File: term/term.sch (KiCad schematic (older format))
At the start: 2 parts

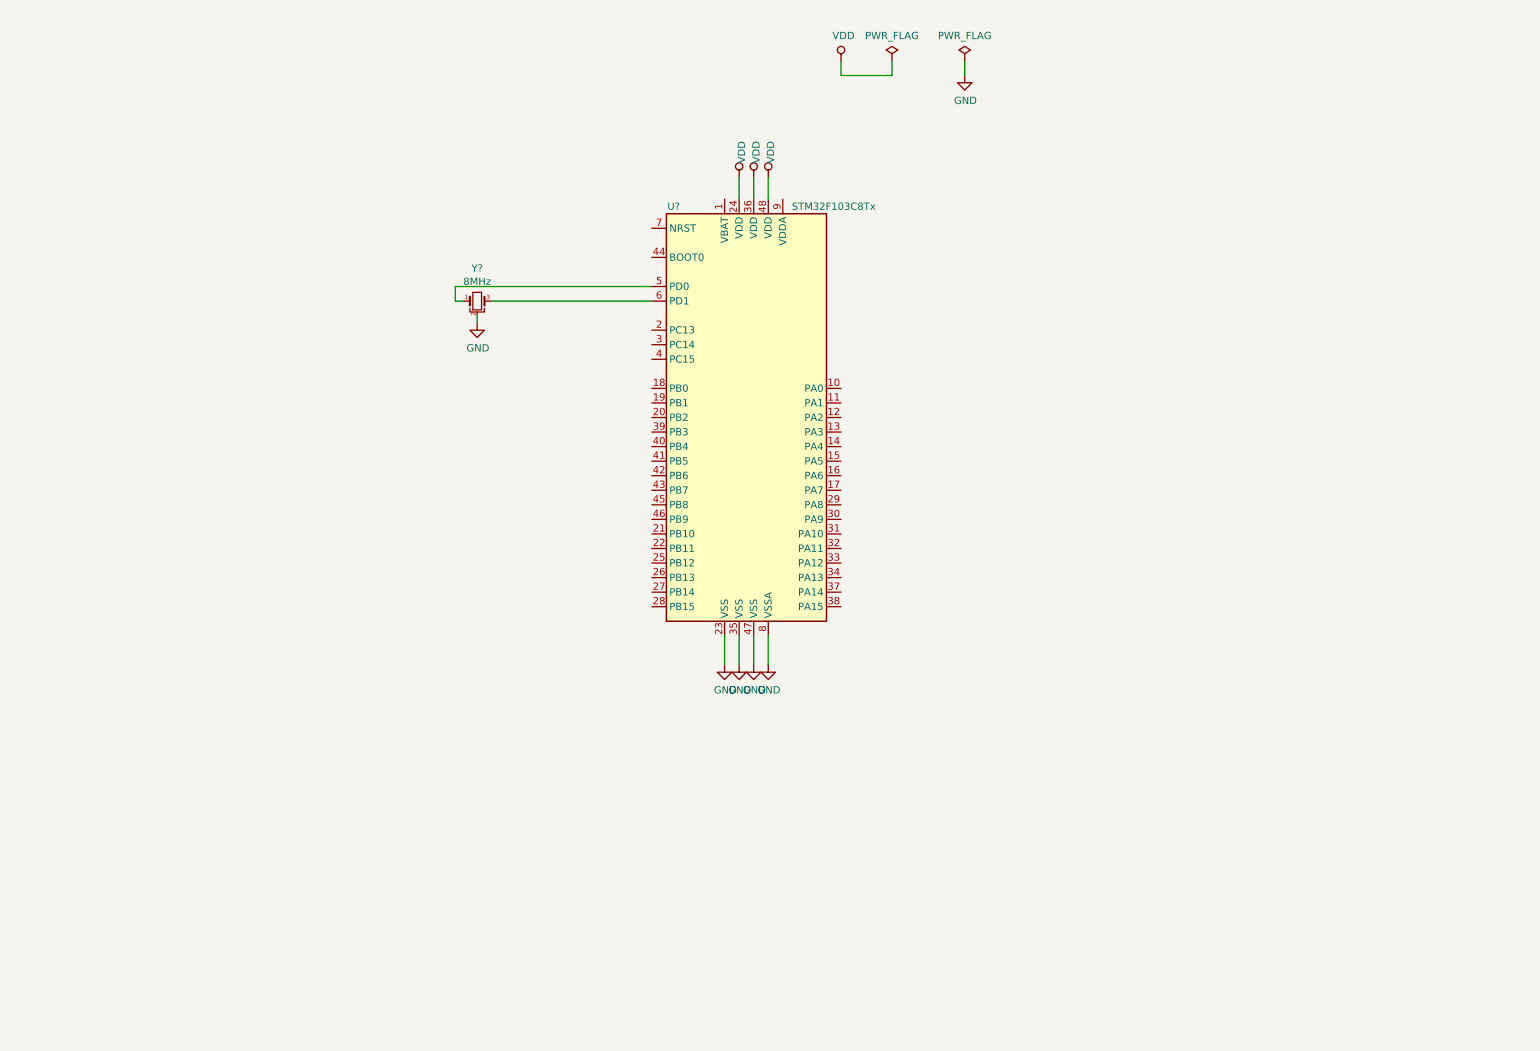
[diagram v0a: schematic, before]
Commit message: Add eeprom functions, i2c functions, save and restore data
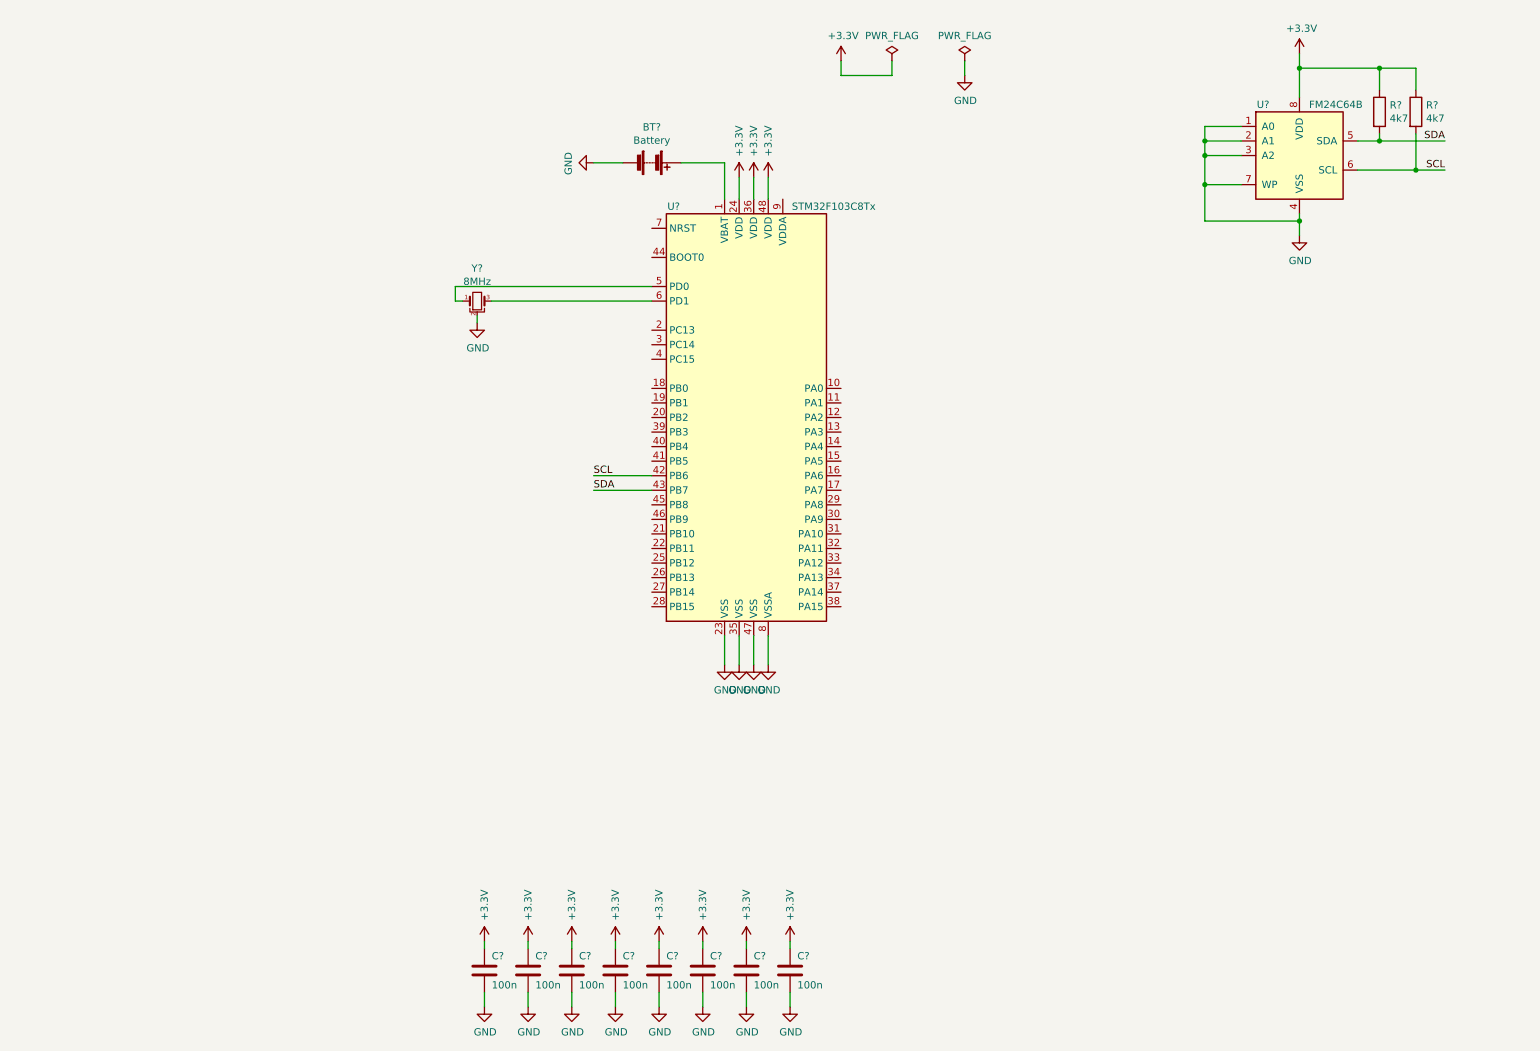
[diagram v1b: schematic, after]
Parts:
- added BT?: Battery, Battery:BatteryHolder_ComfortableElectronic_CH273-2450_1x2450, symbol Device:Battery
- added C? (x8): 100n, Capacitor_SMD:C_0805_2012Metric, symbol Device:C
- added R? (x2): 4k7, Resistor_SMD:R_0805_2012Metric, symbol Device:R
- added U?: FM24C64B, Package_SO:SOIC-8_3.9x4.9mm_P1.27mm, symbol Memory_NVRAM:FM24C64B
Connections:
- net GND: now also BT?.2 (-), C?.2, C?.2, C?.2, C?.2, C?.2, C?.2, C?.2, C?.2, U?.1 (A0), U?.2 (A1), U?.3 (A2), U?.4 (VSS), U?.7 (WP)
- net at U?.1 (VBAT): now also BT?.1 (+)
- net SCL: now reaches U?.42 (PB6)
- net SCL: now also R?.2, U?.6 (SCL)
- net SDA: now reaches U?.43 (PB7)
- net SDA: now also R?.2, U?.5 (SDA)
- net VDD renamed +3V3
- net +3V3: now also C?.1, C?.1, C?.1, C?.1, C?.1, C?.1, C?.1, C?.1, R?.1, R?.1, U?.8 (VDD)

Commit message: Continue schematic draw
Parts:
- removed R? (x2): 4k7, Resistor_SMD:R_0805_2012Metric, symbol Device:R
- added C10: 100n, Capacitor_SMD:C_0805_2012Metric, symbol Device:C_Small
- added C11, C9: 22p, Capacitor_SMD:C_0805_2012Metric, symbol Device:C_Small
- added J1, J2, J3: Conn_01x03_Male, symbol Connector:Conn_01x03_Male
- added J4: Conn_ARM_JTAG_SWD_10, Connector_IDC:IDC-Header_2x05_P2.54mm_Vertical, symbol Connector:Conn_ARM_JTAG_SWD_10
- added R1: 1k, Resistor_SMD:R_0805_2012Metric, symbol Device:R_Small
- added R2, R6, R7: 4k7, Resistor_SMD:R_0805_2012Metric, symbol Device:R_Small
- added R3: 10, Resistor_SMD:R_1210_3225Metric, symbol Device:R_Small
- added R4, R5: 100k, Resistor_SMD:R_0805_2012Metric, symbol Device:R_Small
- added RV1: 10k, symbol Device:R_POT_Small
- added U1: 74HC595, Package_SO:SOIC-16_3.9x9.9mm_P1.27mm, symbol 74xx:74HC595
- added U2: WG12864A, Connector_PinHeader_2.54mm:PinHeader_1x20_P2.54mm_Vertical, symbol lcd:WG12864A
- added Y2: 32678, symbol Device:Crystal_Small
- gave numbers to parts that had none: 12
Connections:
- net +3V3: now also J1.1 (Pin_1), J2.1 (Pin_1), J3.1 (Pin_1), J4.1 (VTref), R2.2, R4.1, R6.1, R7.1
- net GND: now also C10.2, C11.2, C9.1, J1.3 (Pin_3), J2.3 (Pin_3), J3.3 (Pin_3), J4.3 (GND), J4.5 (GND), J4.9 (GNDDetect), R3.2, R5.2, U1.13 (~OE), U1.8 (GND), U2.1 (Vss), U2.5 (R/W)
- net SCL: now also R7.2
- net SDA: now also R6.2
- net KEY_UP: now reaches U3.12 (PA2)
- net KEY_DOWN: now reaches U3.13 (PA3)
- net KEY_LEFT: now reaches U3.14 (PA4)
- net KEY_RIGHT: now reaches U3.15 (PA5)
- net OW: now reaches U3.17 (PA7)
- net OW: now also J1.2 (Pin_2), J2.2 (Pin_2), J3.2 (Pin_2), R2.1
- net LCD_RST: now reaches U3.21 (PB10)
- net LCD_RST: now also U2.17 (~RES)
- net LCD_DI: now reaches U3.22 (PB11)
- net LCD_DI: now also U2.4 (D/I)
- net LCD_CLK: now reaches U3.25 (PB12)
- net LCD_CLK: now also U1.12 (RCLK)
- net LCD_SHIFT: now reaches U3.26 (PB13)
- net LCD_SHIFT: now also U1.11 (SRCLK)
- net LCD_E: now reaches U3.27 (PB14)
- net LCD_E: now also U2.6 (E)
- net LCD_DATA: now reaches U3.28 (PB15)
- net LCD_DATA: now also U1.14 (SER)
- net at U3.3 (PC14): now also C9.2, Y2.2
- net USART1_TX: now reaches U3.30 (PA9)
- net USART1_RX: now reaches U3.31 (PA10)
- net JTMS: now reaches U3.34 (PA13)
- net JTMS: now also J4.2 (SWDIO/TMS)
- net JTCK: now reaches U3.37 (PA14)
- net JTCK: now also J4.4 (SWDCLK/TCK)
- net JTDI: now reaches U3.38 (PA15)
- net JTDI: now also J4.8 (NC/TDI)
- net JTDO: now reaches U3.39 (PB3)
- net JTDO: now also J4.6 (SWO/TDO)
- net at U3.4 (PC15): now also C11.1, Y2.1
- net at U3.44 (BOOT0): now also R5.1
- net LCD_CS1: now reaches U3.45 (PB8)
- net LCD_CS1: now also U2.15 (CS1)
- net LCD_CS2: now reaches U3.46 (PB9)
- net LCD_CS2: now also U2.16 (CS2)
- net NRESET: now reaches U3.7 (NRST)
- net NRESET: now also C10.1, J4.10 (~RESET~), R4.2
- new net: U1.3 (QD), U2.10 (DB3)
- new net: U1.4 (QE), U2.11 (DB4)
- new net: U1.5 (QF), U2.12 (DB5)
- new net: U1.6 (QG), U2.13 (DB6)
- new net: U1.7 (QH), U2.14 (DB7)
- new net: RV1.3, U2.18 (Vout)
- new net: R3.1, U2.20 (K)
- new net: RV1.2, U2.3 (V0)
- new net: U1.15 (QA), U2.7 (DB0)
- new net: U1.1 (QB), U2.8 (DB1)
- new net: U1.2 (QC), U2.9 (DB2)
- new net: R1.2, U1.10 (~SRCLR)
- new net VCC: R1.1, RV1.1, U1.16 (VCC), U2.19 (A), U2.2 (Vdd)
- no-connect marks 0 -> 10
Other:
- moved on the sheet: BT1, U3, U4, Y1

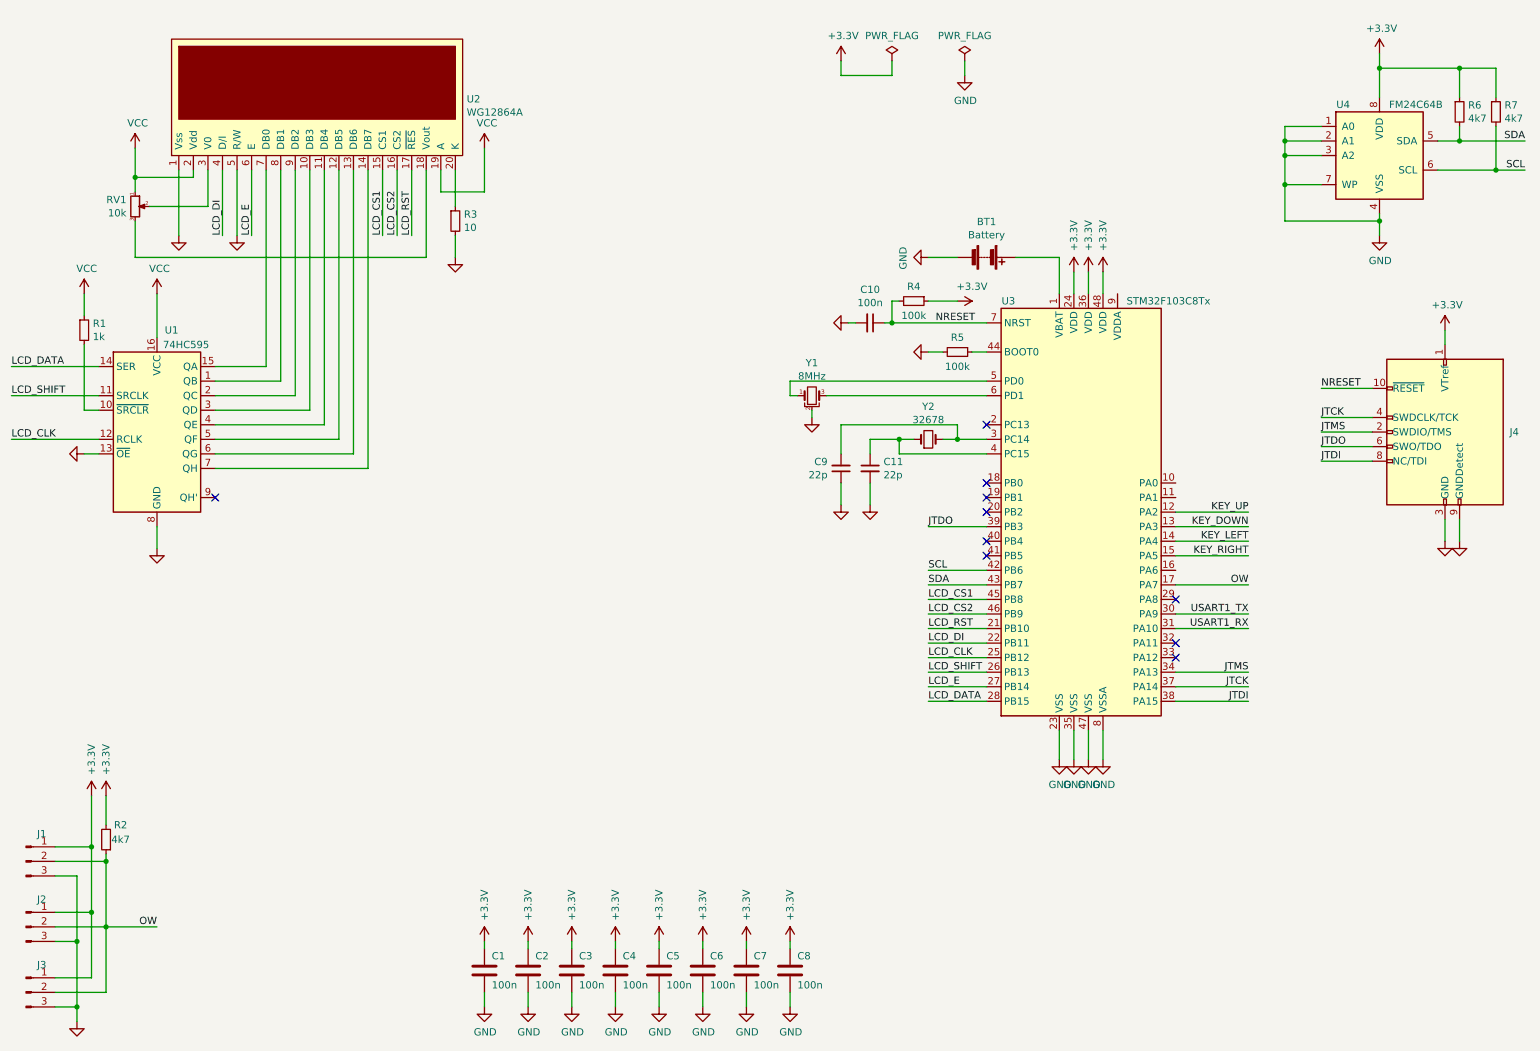
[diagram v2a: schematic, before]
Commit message: Add kicad project with stm32 module
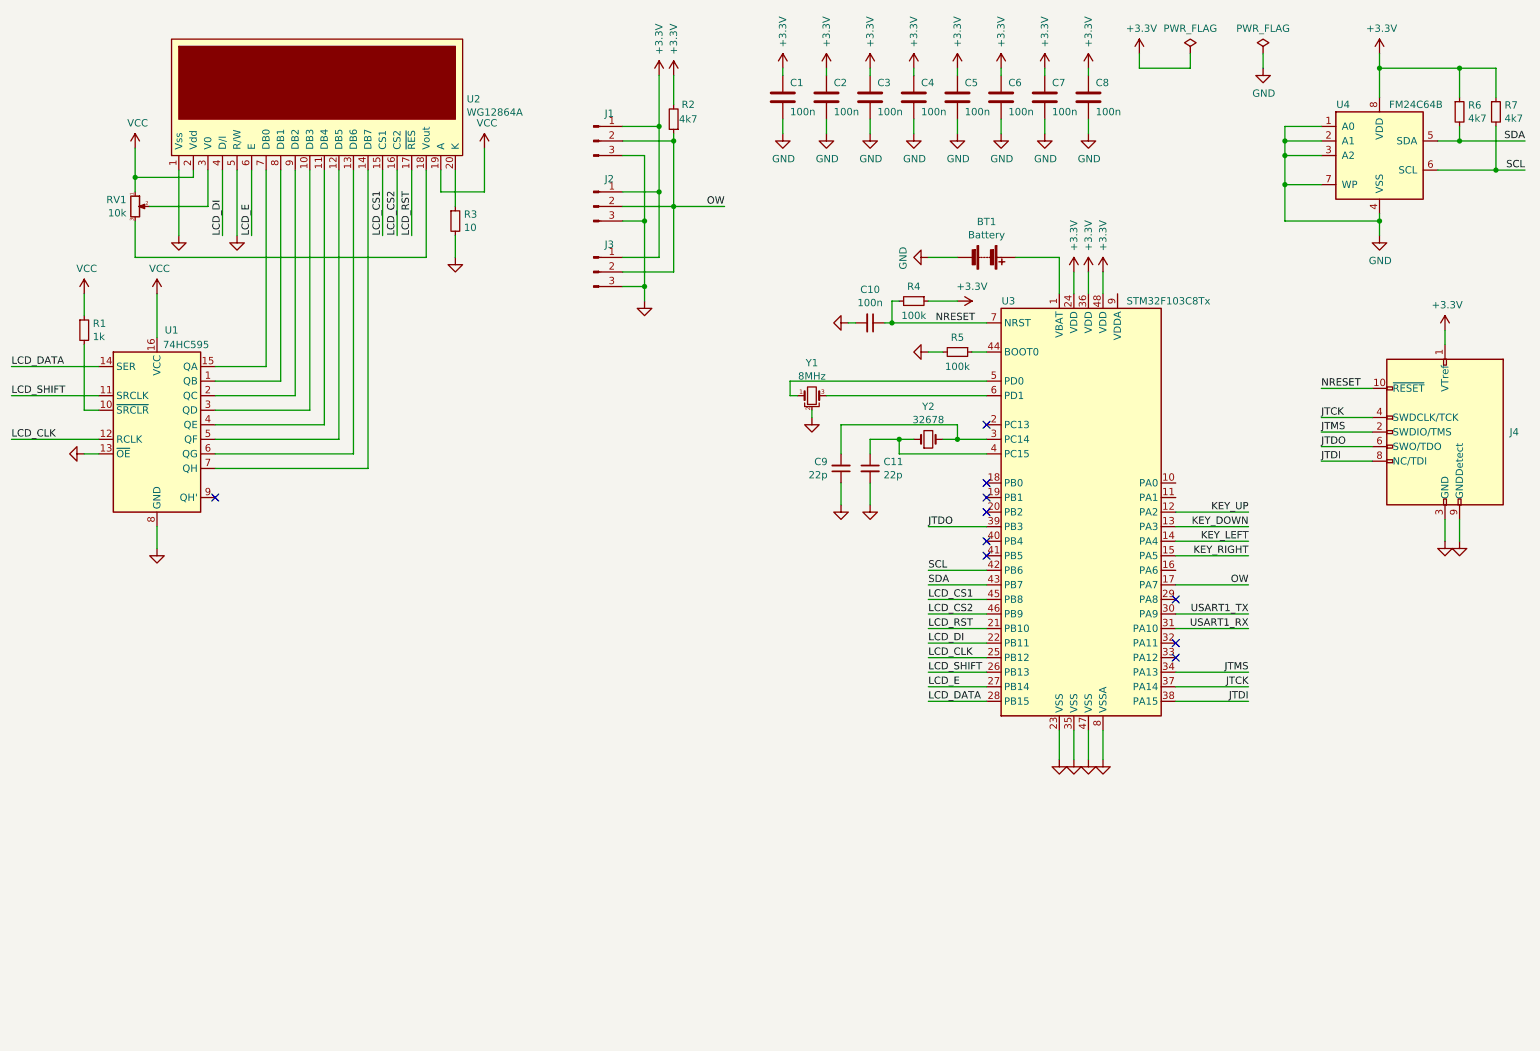
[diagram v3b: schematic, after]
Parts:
- RV1: footprint (none) -> Potentiometer_THT:Potentiometer_ACP_CA9-V10_Vertical
- Y1: footprint (none) -> Crystal:Resonator_SMD_muRata_CSTxExxV-3Pin_3.0x1.1mm
- Y2: footprint (none) -> Crystal:Crystal_SMD_3215-2Pin_3.2x1.5mm
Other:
- moved on the sheet: C1, C2, C3, C4, C5, C6, C7, C8, J1, J2, J3, R2
